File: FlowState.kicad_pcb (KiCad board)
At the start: 2 copper layers, 54.5 x 58.2 mm, 13 parts, among them J1 USB_C_Receptacle_USB2.0_16P, J2 Conn_01x04_Pin (CO2), J3 Conn_01x14_Pin(LCD), J4 Conn_01x03_Pin (SOIL), J5 Conn_01x04_Pin(SD), J6 Conn_01x02_Pin(Switch), U1 AMS1117-3.3, U2 ESP32-DEVKIT-V1

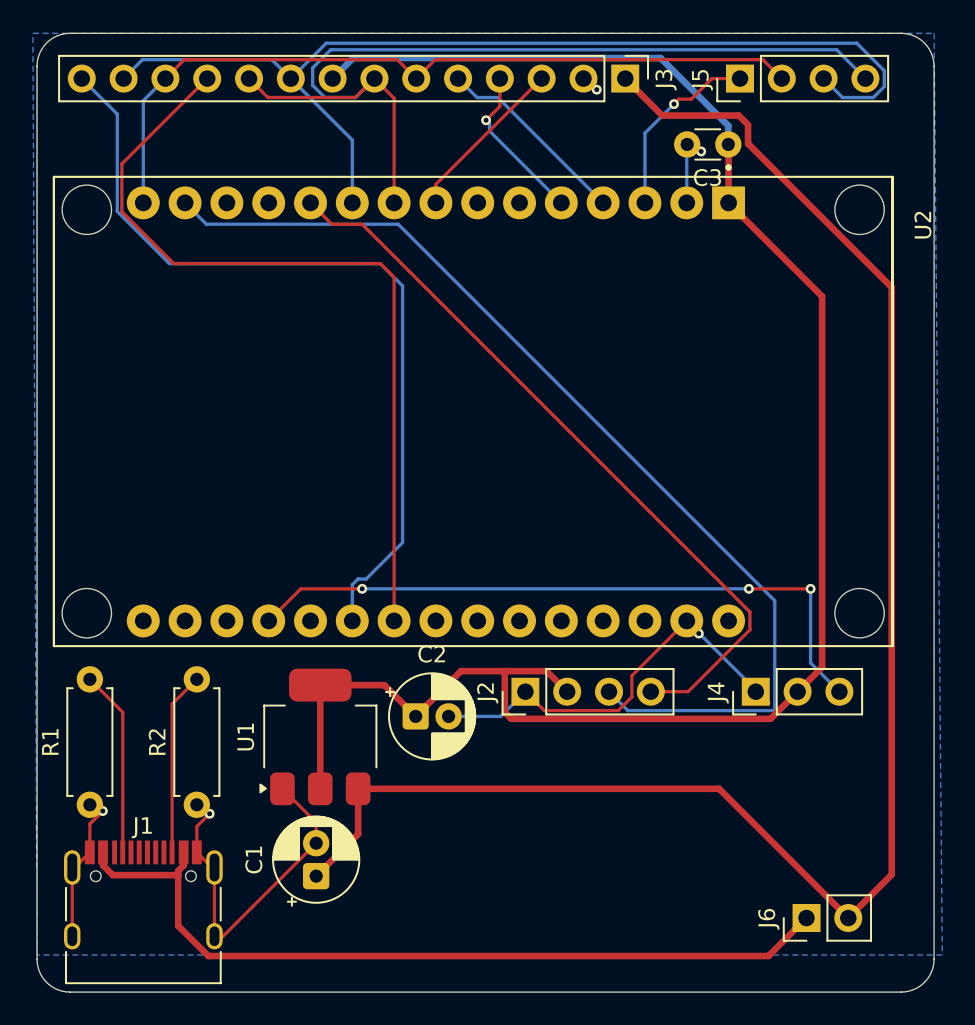
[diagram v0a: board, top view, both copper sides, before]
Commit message: edits
rewired LCD to differnt GPIO because that pin has HIGH voltage at startup
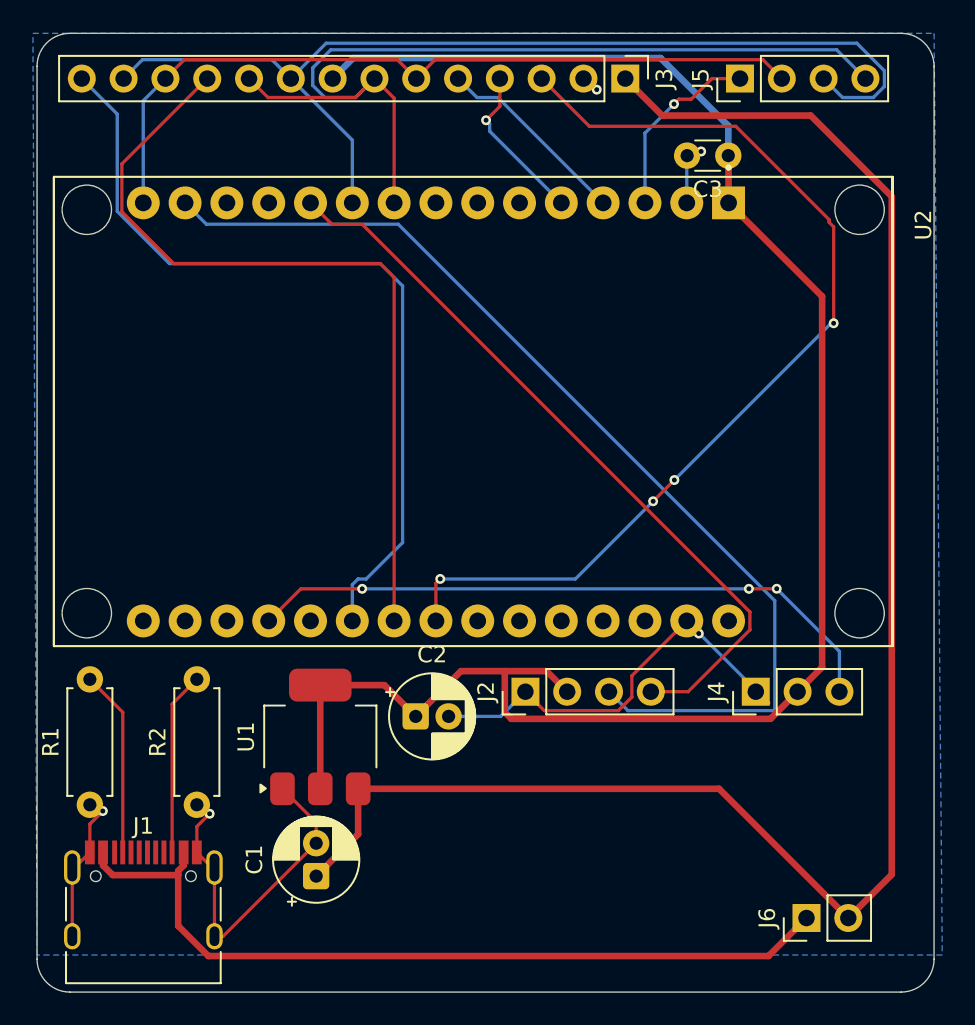
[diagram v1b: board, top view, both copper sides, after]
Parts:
- moved C3 0.68 mm to (57.0, 20.9)
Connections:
- U2 pad 23: unconnected-(U2-D25-Pad23) -> LCD_CS
- U2 pad 8: LCD_CS -> unconnected-(U2-D5-Pad8)
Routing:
- net LCD_CS: track 10.2 -> 60.4 mm, vias 0 -> 4
- net VCC_5V: track 100.9 -> 103.5 mm
- net SOIL_SIG: track 40.7 -> 39.5 mm
- net GND: track 63.8 -> 63.1 mm
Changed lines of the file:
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@@
 	(net 7 "unconnected-(U2-EN-Pad16)")
 	(net 8 "unconnected-(U2-D14-Pad26)")
-	(net 9 "unconnected-(U2-D25-Pad23)")
+	(net 9 "unconnected-(U2-D5-Pad8)")
 	(net 10 "LCD_CS")
 	(net 11 "SOIL_SIG")
@@
 	(footprint "Capacitor_THT:C_Disc_D3.0mm_W1.6mm_P2.50mm"
 		(layer "F.Cu")
-		(at 57 20.25 180)
+		(at 56.9976 20.9296 180)
 		(descr "C, Disc series, Radial, pin pitch=2.50mm, diameter*width=3.0*1.6mm^2, Capacitor, http://www.vishay.com/docs/45233/krseries.pdf")
 		(tags "C Disc series Radial pin pitch 2.50mm diameter 3.0mm width 1.6mm Capacitor")
@@
 			(layers "*.Cu" "*.Mask")
 			(remove_unused_layers no)
-			(net 10 "LCD_CS")
+			(net 9 "unconnected-(U2-D5-Pad8)")
 			(pinfunction "D5")
-			(pintype "bidirectional")
+			(pintype "bidirectional+no_connect")
 			(solder_mask_margin 0.102)
 		)
@@
 			(layers "*.Cu" "*.Mask")
 			(remove_unused_layers no)
-			(net 9 "unconnected-(U2-D25-Pad23)")
+			(net 10 "LCD_CS")
 			(pinfunction "D25")
-			(pintype "bidirectional+no_connect")
+			(pintype "bidirectional")
 			(solder_mask_margin 0.102)
 		)
@@
 	)
 	(segment
+		(start 54.4976 20.9296)
+		(end 54.4976 20.8304)
+		(width 0.2)
+		(layer "F.Cu")
+		(net 1)
+	)
+	(segment
 		(start 24.71 60.37)
 		(end 24.940197 60.37)
@@
 	)
 	(segment
-		(start 31.96 62.705111)
-		(end 26.305111 68.36)
+		(start 54.4976 20.8304)
+		(end 54.653147 20.674853)
 		(width 0.2)
 		(layer "F.Cu")
@@
 	)
 	(segment
-		(start 54.5 20.25)
-		(end 54.924853 20.25)
+		(start 31.96 62.705111)
+		(end 26.305111 68.36)
 		(width 0.2)
 		(layer "F.Cu")
@@
 	)
 	(segment
-		(start 54.924853 20.25)
+		(start 54.653147 20.674853)
 		(end 55.349706 20.674853)
 		(width 0.2)
@@
 	)
 	(segment
+		(start 54.475 20.9522)
+		(end 54.4976 20.9296)
+		(width 0.2)
+		(layer "B.Cu")
+		(net 1)
+	)
+	(segment
 		(start 40.004889 55)
 		(end 43.17 55)
@@
 	(segment
 		(start 54.475 23.799999)
-		(end 54.475 20.275)
-		(width 0.2)
-		(layer "B.Cu")
-		(net 1)
-	)
-	(segment
-		(start 54.475 20.275)
-		(end 54.5 20.25)
+		(end 54.475 20.9522)
 		(width 0.2)
 		(layer "B.Cu")
@@
 	)
 	(segment
-		(start 52.989265 18.499265)
-		(end 50.74 16.25)
-		(width 0.4)
-		(layer "F.Cu")
-		(net 2)
-	)
-	(segment
-		(start 64.29 67.25)
-		(end 66.929 64.611)
+		(start 62.011981 18.499265)
+		(end 66.929 23.416284)
 		(width 0.4)
 		(layer "F.Cu")
@@
 	)
 	(segment
-		(start 66.929 28.931716)
-		(end 58.2 20.202716)
+		(start 50.74 16.25)
+		(end 52.989265 18.499265)
 		(width 0.4)
 		(layer "F.Cu")
@@
 	)
 	(segment
-		(start 58.2 19.058)
-		(end 57.641265 18.499265)
-		(width 0.4)
-		(layer "F.Cu")
-		(net 2)
-	)
-	(segment
-		(start 58.2 20.202716)
-		(end 58.2 19.058)
+		(start 64.29 67.25)
+		(end 56.44 59.4)
 		(width 0.4)
 		(layer "F.Cu")
@@
 	)
 	(segment
-		(start 57.641265 18.499265)
-		(end 52.989265 18.499265)
+		(start 66.929 23.416284)
+		(end 66.929 64.611)
 		(width 0.4)
 		(layer "F.Cu")
@@
 	)
 	(segment
-		(start 64.29 67.25)
-		(end 56.44 59.4)
+		(start 31.96 64.705112)
+		(end 34.51 62.155112)
 		(width 0.4)
 		(layer "F.Cu")
@@
 	)
 	(segment
-		(start 31.96 64.705112)
-		(end 34.51 62.155112)
+		(start 52.989265 18.499265)
+		(end 62.011981 18.499265)
 		(width 0.4)
 		(layer "F.Cu")
@@
 	(segment
 		(start 66.929 64.611)
-		(end 66.929 28.931716)
+		(end 64.29 67.25)
 		(width 0.4)
 		(layer "F.Cu")
@@
 	(segment
 		(start 45.660001 16.25)
-		(end 39.235 22.675001)
+		(end 48.560001 19.15)
+		(width 0.2)
+		(layer "F.Cu")
+		(net 10)
+	)
+	(segment
+		(start 48.560001 19.15)
+		(end 57.455635 19.15)
 		(width 0.2)
 		(layer "F.Cu")
@@
 	)
 	(segment
-		(start 39.235 22.675001)
-		(end 39.235 23.8)
+		(start 39.235 46.912)
+		(end 39.235 49.2)
 		(width 0.2)
 		(layer "F.Cu")
@@
 	)
 	(segment
+		(start 63.125 24.819365)
+		(end 63.125 24.986295)
+		(width 0.2)
+		(layer "F.Cu")
+		(net 10)
+	)
+	(segment
+		(start 53.721 40.64)
+		(end 52.431504 41.929496)
+		(width 0.2)
+		(layer "F.Cu")
+		(net 10)
+	)
+	(segment
+		(start 39.497 46.65)
+		(end 39.235 46.912)
+		(width 0.2)
+		(layer "F.Cu")
+		(net 10)
+	)
+	(segment
+		(start 57.455635 19.15)
+		(end 63.125 24.819365)
+		(width 0.2)
+		(layer "F.Cu")
+		(net 10)
+	)
+	(segment
+		(start 63.4 25.261295)
+		(end 63.4 31.115)
+		(width 0.2)
+		(layer "F.Cu")
+		(net 10)
+	)
+	(segment
+		(start 63.125 24.986295)
+		(end 63.4 25.261295)
+		(width 0.2)
+		(layer "F.Cu")
+		(net 10)
+	)
+	(via
+		(at 39.497 46.65)
+		(size 0.6)
+		(drill 0.3)
+		(layers "F.Cu" "B.Cu")
+		(net 10)
+	)
+	(via
+		(at 52.431504 41.929496)
+		(size 0.6)
+		(drill 0.3)
+		(layers "F.Cu" "B.Cu")
+		(net 10)
+	)
+	(via
+		(at 63.4 31.115)
+		(size 0.6)
+		(drill 0.3)
+		(layers "F.Cu" "B.Cu")
+		(net 10)
+	)
+	(via
+		(at 53.721 40.64)
+		(size 0.6)
+		(drill 0.3)
+		(layers "F.Cu" "B.Cu")
+		(net 10)
+	)
+	(segment
+		(start 63.246 31.115)
+		(end 53.721 40.64)
+		(width 0.2)
+		(layer "B.Cu")
+		(net 10)
+	)
+	(segment
+		(start 47.711 46.65)
+		(end 39.497 46.65)
+		(width 0.2)
+		(layer "B.Cu")
+		(net 10)
+	)
+	(segment
+		(start 63.4 31.115)
+		(end 63.246 31.115)
+		(width 0.2)
+		(layer "B.Cu")
+		(net 10)
+	)
+	(segment
+		(start 52.431504 41.929496)
+		(end 47.711 46.65)
+		(width 0.2)
+		(layer "B.Cu")
+		(net 10)
+	)
+	(segment
 		(start 31.025 47.25)
 		(end 29.075 49.2)
@@
 	)
 	(segment
-		(start 62 47.25)
+		(start 58.254529 47.245471)
 		(end 58.25 47.25)
 		(width 0.2)
@@
 		(net 11)
 	)
+	(segment
+		(start 59.942529 47.245471)
+		(end 58.254529 47.245471)
+		(width 0.2)
+		(layer "F.Cu")
+		(net 11)
+	)
 	(via
 		(at 58.25 47.25)
@@
 	)
 	(via
-		(at 34.755 47.25)
+		(at 59.942529 47.245471)
 		(size 0.6)
 		(drill 0.3)
@@
 	)
 	(via
-		(at 62 47.25)
+		(at 34.755 47.25)
 		(size 0.6)
 		(drill 0.3)
@@
 	)
 	(segment
-		(start 62 51.750001)
-		(end 62 47.25)
+		(start 63.749999 53.5)
+		(end 63.749999 51.052941)
 		(width 0.2)
 		(layer "B.Cu")
@@
 	)
 	(segment
-		(start 63.749999 53.5)
-		(end 62 51.750001)
+		(start 58.25 47.25)
+		(end 34.755 47.25)
 		(width 0.2)
 		(layer "B.Cu")
@@
 	)
 	(segment
-		(start 58.25 47.25)
-		(end 34.755 47.25)
+		(start 63.749999 51.052941)
+		(end 59.942529 47.245471)
 		(width 0.2)
 		(layer "B.Cu")
@@
 	)
 	(segment
-		(start 57.015 20.265)
-		(end 57 20.25)
-		(width 0.4)
-		(layer "F.Cu")
-		(net 25)
-	)
-	(segment
 		(start 40.754888 52.25)
 		(end 43.434 52.25)
@@
 	)
 	(segment
+		(start 57.015 23.8)
+		(end 57.015 20.947)
+		(width 0.4)
+		(layer "F.Cu")
+		(net 25)
+	)
+	(segment
 		(start 62.7 52.01)
 		(end 62.7 29.485)
@@
 	)
 	(segment
-		(start 57.015 23.8)
-		(end 57.015 20.265)
+		(start 38.004888 55)
+		(end 40.754888 52.25)
 		(width 0.4)
 		(layer "F.Cu")
@@
 	)
 	(segment
-		(start 38.004888 55)
-		(end 40.754888 52.25)
+		(start 45.96 52.25)
+		(end 47.21 53.5)
 		(width 0.4)
 		(layer "F.Cu")
@@
 	)
 	(segment
-		(start 45.96 52.25)
-		(end 47.21 53.5)
+		(start 57.015 20.947)
+		(end 56.9976 20.9296)
 		(width 0.4)
 		(layer "F.Cu")
@@
 	)
 	(segment
-		(start 34.209999 15)
-		(end 32.959999 16.25)
+		(start 57 19.11863)
+		(end 52.88137 15)
 		(width 0.4)
 		(layer "B.Cu")
@@
 	)
 	(segment
-		(start 52.88137 15)
-		(end 34.209999 15)
+		(start 56.9976 20.9296)
+		(end 57 20.9272)
 		(width 0.4)
 		(layer "B.Cu")
@@
 	)
 	(segment
-		(start 57 20.25)
-		(end 57 19.11863)
+		(start 34.209999 15)
+		(end 32.959999 16.25)
 		(width 0.4)
 		(layer "B.Cu")
@@
 	)
 	(segment
-		(start 57 19.11863)
-		(end 52.88137 15)
+		(start 52.88137 15)
+		(end 34.209999 15)
+		(width 0.4)
+		(layer "B.Cu")
+		(net 25)
+	)
+	(segment
+		(start 57 20.9272)
+		(end 57 19.11863)
 		(width 0.4)
 		(layer "B.Cu")
